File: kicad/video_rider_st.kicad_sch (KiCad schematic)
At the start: 37 parts, among them J1 F3311A7H121020E200, J2 F3311A7H121020E200, J3 Conn_01x02_Male, J4 Conn_01x03_Male, J5 F3311A7H121020E200, J6 F3311A7H121020E200, J7 Conn_01x06_Male, U1 ST_SHIFTER_PHY, U10 ST_GLUE_SOCKET, U2 ST_SHIFTER_SOCKET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

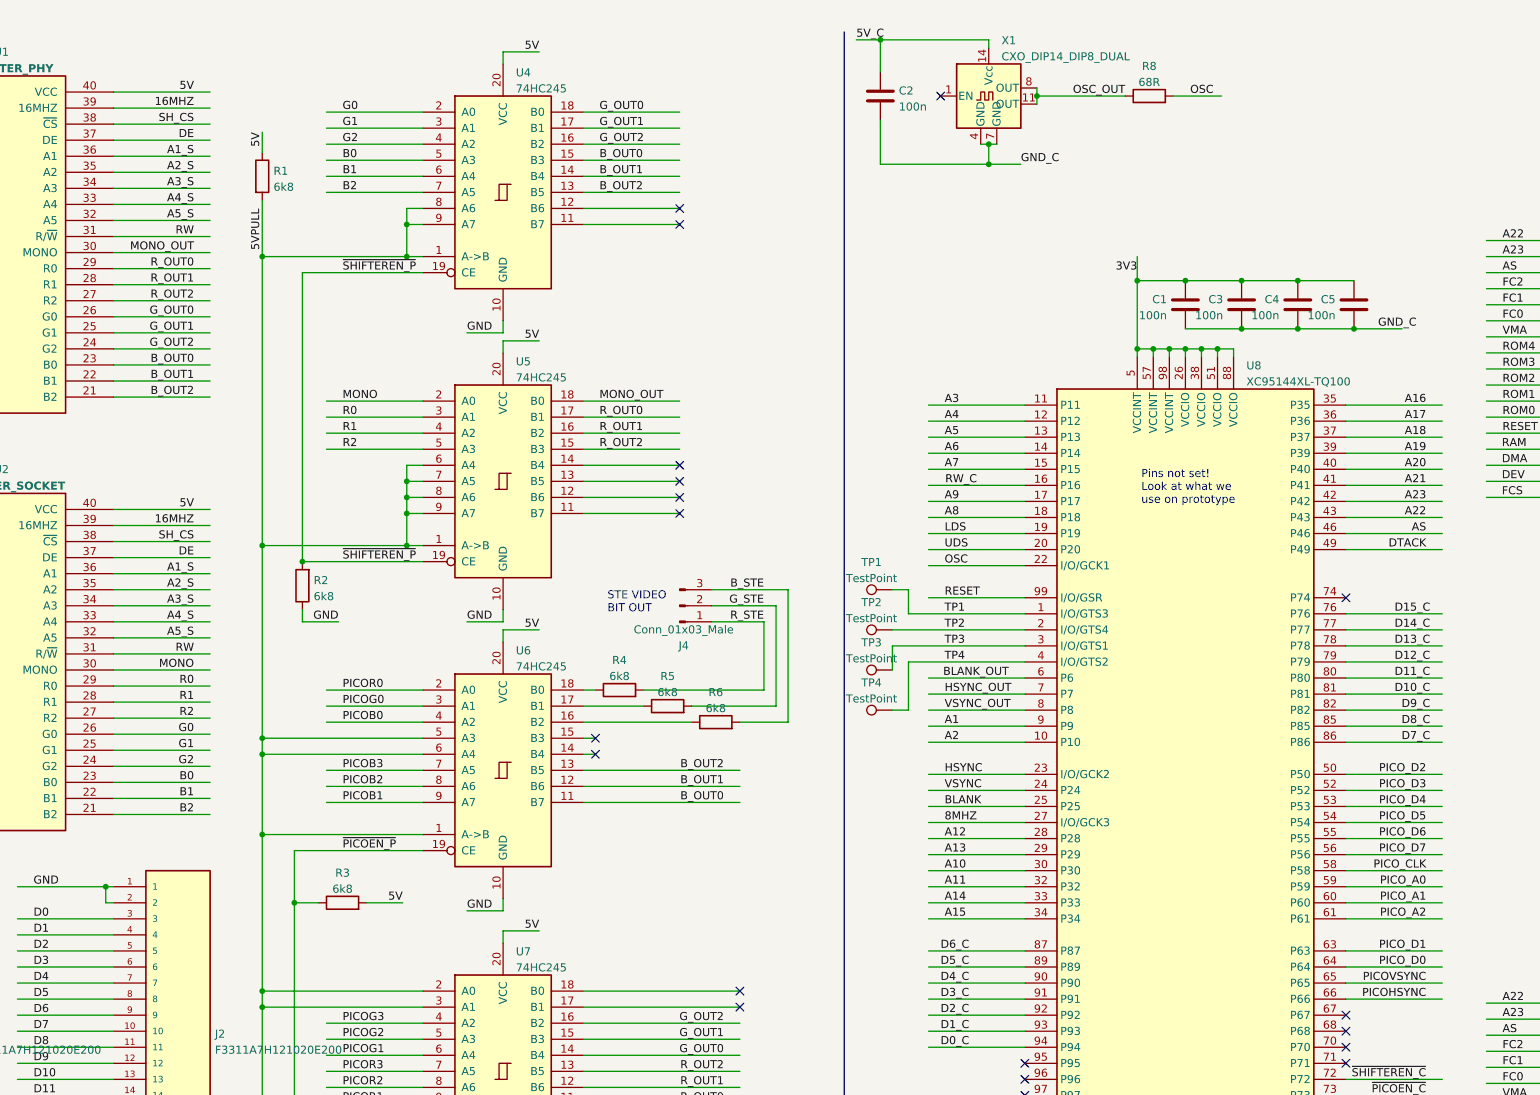
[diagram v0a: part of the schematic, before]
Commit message: Just about ready to order, but need to check the dual dip library.
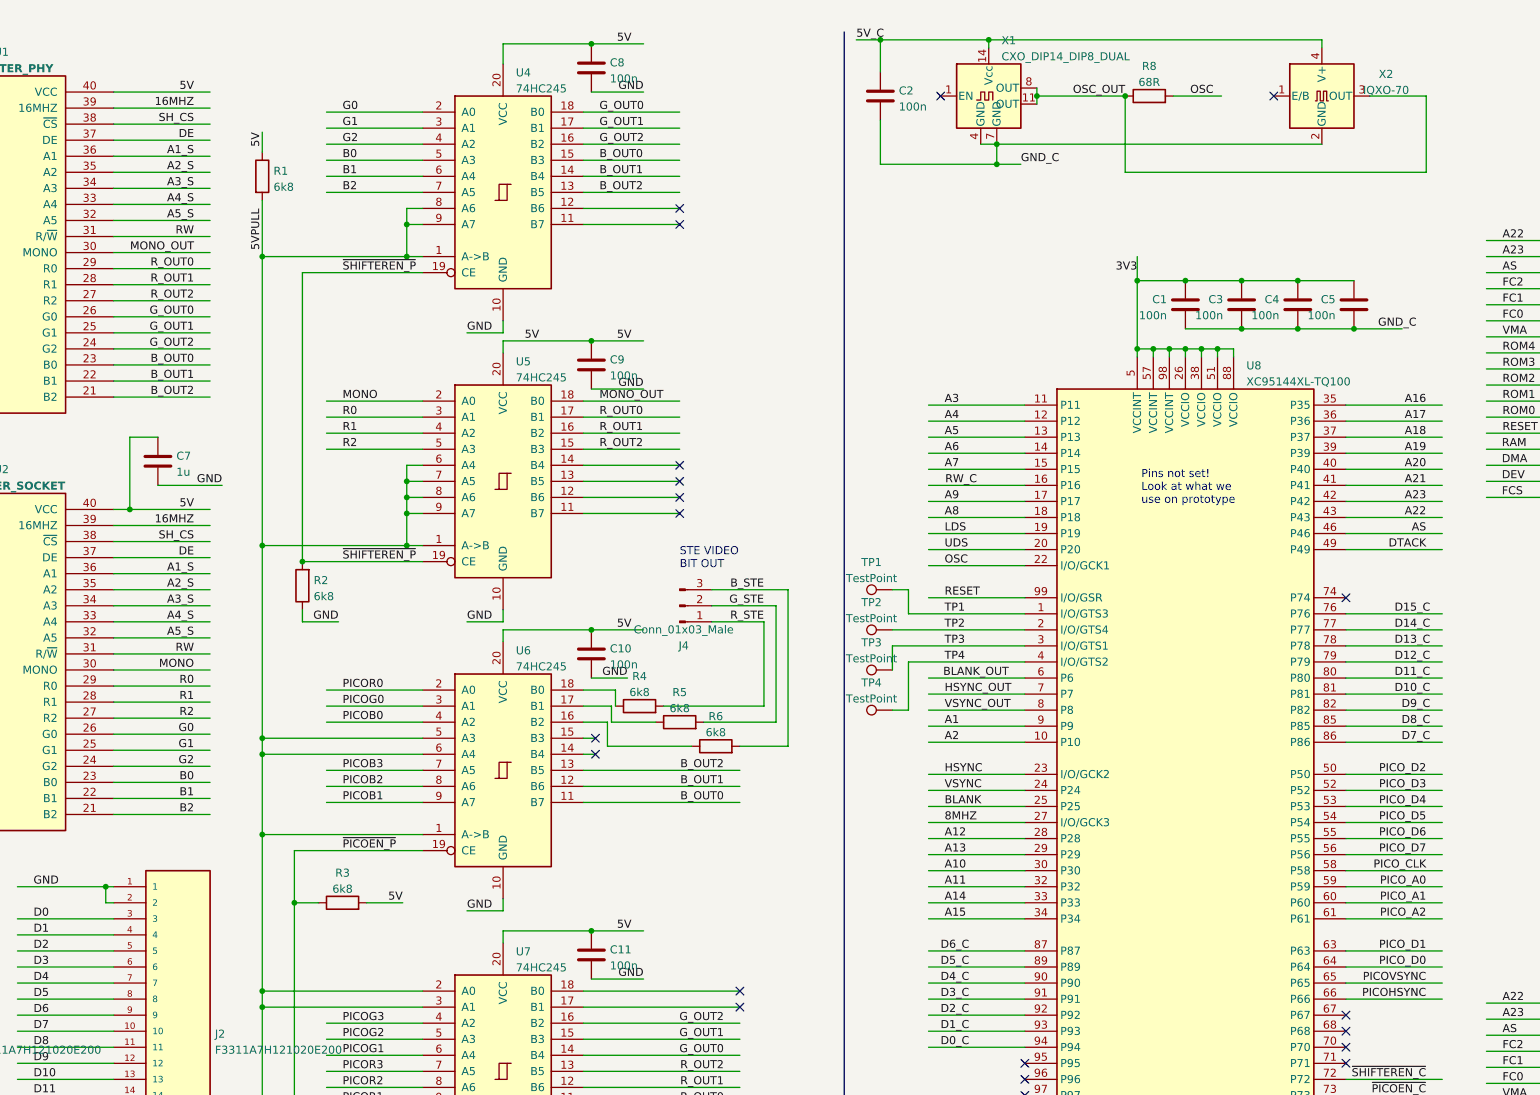
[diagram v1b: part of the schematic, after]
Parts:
- added C10, C11, C8, C9: 100n, Capacitor_SMD:C_0805_2012Metric_Pad1.18x1.45mm_HandSolder, symbol Device:C
- added C7: 1u, Capacitor_SMD:C_0805_2012Metric_Pad1.18x1.45mm_HandSolder, symbol Device:C
- added X2: IQXO-70, Oscillator:Oscillator_SMD_IQD_IQXO70-4Pin_7.5x5.0mm, symbol Oscillator:IQXO-70
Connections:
- net 5V: now also C10.1, C11.1, C7.1, C8.1, C9.1
- net 5V_C: now also X2.4 (V+)
- net GND: now also C10.2, C11.2, C7.2, C8.2, C9.2
- net GND_C: now also X2.2 (GND)
- net OSC_OUT: now also X2.3 (OUT)
- no-connect marks 27 -> 28
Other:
- moved on the sheet: R4, R5, R6

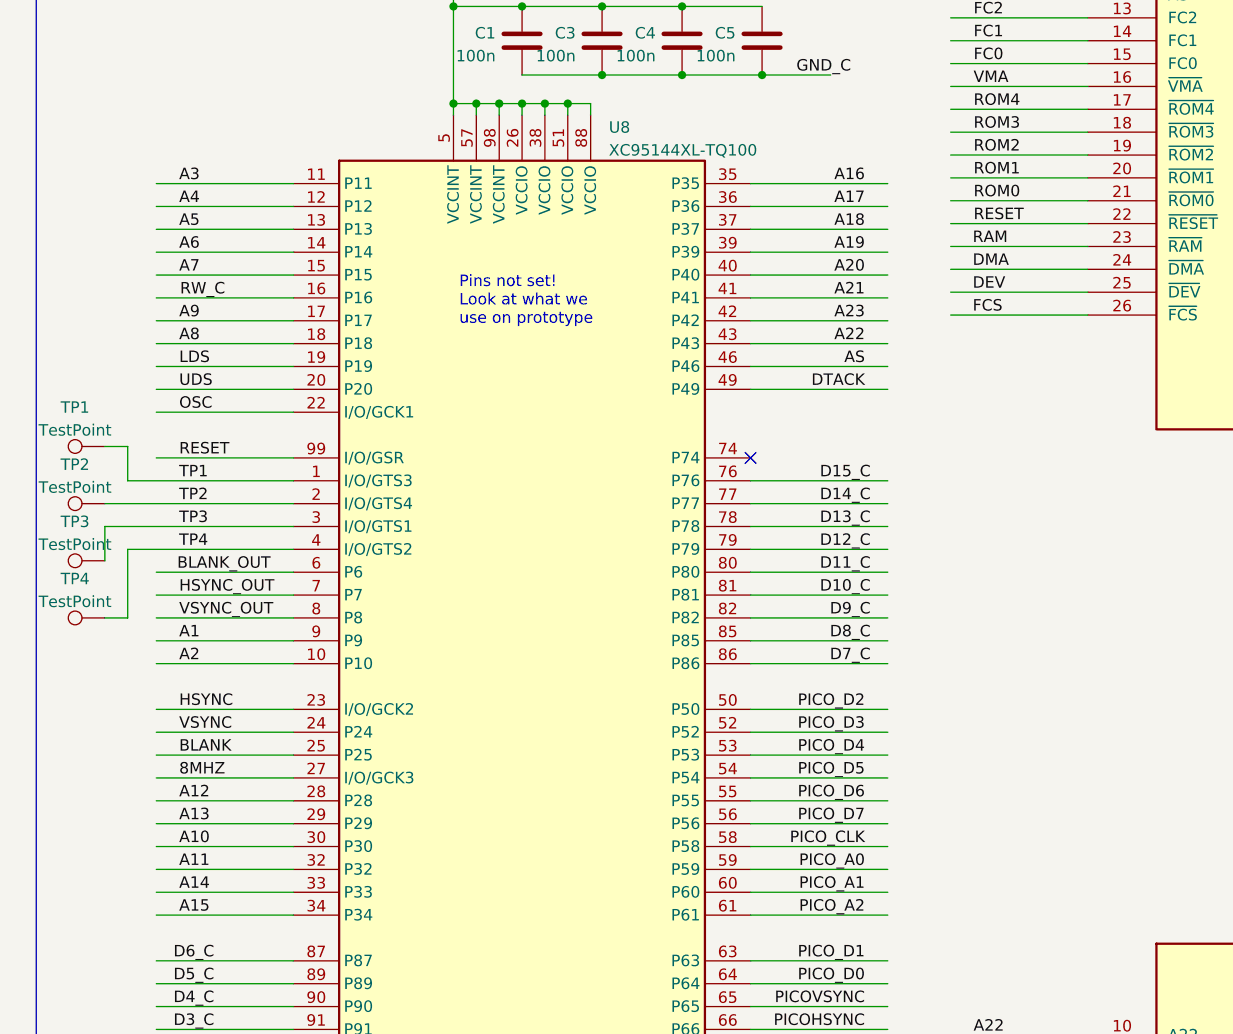
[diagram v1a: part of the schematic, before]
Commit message: Passing DRC with corrected PLCC orientation.
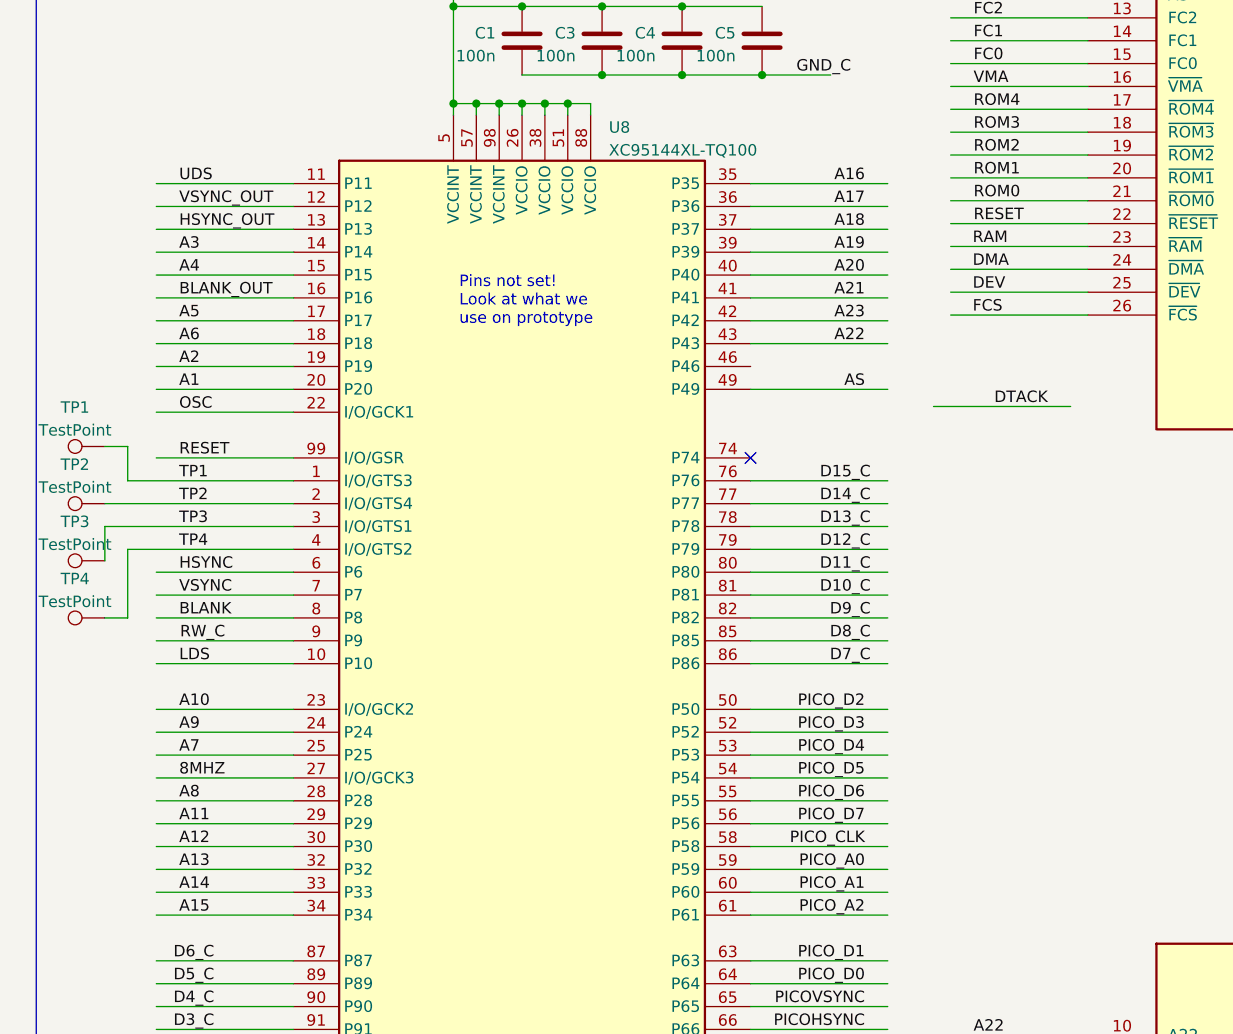
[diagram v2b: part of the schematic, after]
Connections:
- net A1: now also U8.20 (P20); no longer U8.9 (P9)
- net A10: now also U8.23 (I/O/GCK2); no longer U8.30 (P30)
- net A11: now also U8.29 (P29); no longer U8.32 (P32)
- net A12: now also U8.30 (P30); no longer U8.28 (P28)
- net A13: now also U8.32 (P32); no longer U8.29 (P29)
- net A2: now also U8.19 (P19); no longer U8.10 (P10)
- net A3: now also U8.14 (P14); no longer U8.11 (P11)
- net A4: now also U8.15 (P15); no longer U8.12 (P12)
- net A5: now also U8.17 (P17); no longer U8.13 (P13)
- net A6: now also U8.18 (P18); no longer U8.14 (P14)
- net A7: now also U8.25 (P25); no longer U8.15 (P15)
- net A8: now also U8.28 (P28); no longer U8.18 (P18)
- net A9: now also U8.24 (P24); no longer U8.17 (P17)
- net AS: now also U8.49 (P49); no longer U8.46 (P46)
- net BLANK: now also U8.8 (P8); no longer U8.25 (P25)
- net BLANK_OUT: now also U8.16 (P16); no longer U8.6 (P6)
- net DTACK: no longer U8.49 (P49)
- net HSYNC: now also U8.6 (P6); no longer U8.23 (I/O/GCK2)
- net HSYNC_OUT: now also U8.13 (P13); no longer U8.7 (P7)
- net LDS: now also U8.10 (P10); no longer U8.19 (P19)
- net RW_C: now also U8.9 (P9); no longer U8.16 (P16)
- net UDS: now also U8.11 (P11); no longer U8.20 (P20)
- net VSYNC: now also U8.7 (P7); no longer U8.24 (P24)
- net VSYNC_OUT: now also U8.12 (P12); no longer U8.8 (P8)
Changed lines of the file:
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@@
     (stroke (width 0) (type default) (color 0 0 0 0))
   )
-  (wire (pts (xy 269.875 95.25) (xy 285.115 95.25))
+  (wire (pts (xy 269.875 97.79) (xy 285.115 97.79))
     (stroke (width 0) (type default) (color 0 0 0 0))
   )
@@
     (stroke (width 0) (type default) (color 0 0 0 0))
   )
-  (wire (pts (xy 269.875 97.79) (xy 285.115 97.79))
+  (wire (pts (xy 290.195 99.695) (xy 305.435 99.695))
     (stroke (width 0) (type default) (color 0 0 0 0))
   )
@@
     (effects (font (size 1.27 1.27)) (justify right bottom))
   )
-  (label "A12" (at 206.375 143.51 0)
+  (label "A12" (at 206.375 148.59 0)
     (effects (font (size 1.27 1.27)) (justify left bottom))
   )
@@
     (effects (font (size 1.27 1.27)) (justify left bottom))
   )
-  (label "A2" (at 206.375 128.27 0)
+  (label "A2" (at 206.375 95.25 0)
     (effects (font (size 1.27 1.27)) (justify left bottom))
   )
@@
     (effects (font (size 1.27 1.27)) (justify left bottom))
   )
-  (label "BLANK_OUT" (at 216.535 118.11 180)
-    (effects (font (size 1.27 1.27)) (justify right bottom))
+  (label "BLANK_OUT" (at 206.375 87.63 0)
+    (effects (font (size 1.27 1.27)) (justify left bottom))
   )
   (label "D5" (at 62.23 168.91 0)
@@
     (effects (font (size 1.27 1.27)) (justify left bottom))
   )
-  (label "A11" (at 206.375 151.13 0)
+  (label "A11" (at 206.375 146.05 0)
     (effects (font (size 1.27 1.27)) (justify left bottom))
   )
@@
     (effects (font (size 1.27 1.27)) (justify left bottom))
   )
-  (label "HSYNC" (at 206.375 133.35 0)
+  (label "HSYNC" (at 206.375 118.11 0)
     (effects (font (size 1.27 1.27)) (justify left bottom))
   )
@@
     (effects (font (size 1.27 1.27)) (justify left bottom))
   )
-  (label "AS" (at 282.575 95.25 180)
+  (label "AS" (at 282.575 97.79 180)
     (effects (font (size 1.27 1.27)) (justify right bottom))
   )
@@
     (effects (font (size 1.27 1.27)) (justify right bottom))
   )
-  (label "BLANK" (at 206.375 138.43 0)
+  (label "BLANK" (at 206.375 123.19 0)
     (effects (font (size 1.27 1.27)) (justify left bottom))
   )
@@
     (effects (font (size 1.27 1.27)) (justify left bottom))
   )
-  (label "A1" (at 206.375 125.73 0)
+  (label "A1" (at 206.375 97.79 0)
     (effects (font (size 1.27 1.27)) (justify left bottom))
   )
@@
     (effects (font (size 1.27 1.27)) (justify left bottom))
   )
-  (label "A4" (at 206.375 77.47 0)
+  (label "A4" (at 206.375 85.09 0)
     (effects (font (size 1.27 1.27)) (justify left bottom))
   )
@@
     (effects (font (size 1.27 1.27)) (justify right bottom))
   )
-  (label "VSYNC" (at 206.375 135.89 0)
+  (label "VSYNC" (at 206.375 120.65 0)
     (effects (font (size 1.27 1.27)) (justify left bottom))
   )
@@
     (effects (font (size 1.27 1.27)) (justify left bottom))
   )
-  (label "A5" (at 206.375 80.01 0)
+  (label "A5" (at 206.375 90.17 0)
     (effects (font (size 1.27 1.27)) (justify left bottom))
   )
@@
     (effects (font (size 1.27 1.27)) (justify left bottom))
   )
-  (label "VSYNC_OUT" (at 206.375 123.19 0)
+  (label "VSYNC_OUT" (at 206.375 77.47 0)
     (effects (font (size 1.27 1.27)) (justify left bottom))
   )
@@
     (effects (font (size 1.27 1.27)) (justify right bottom))
   )
-  (label "RW_C" (at 206.4754 87.63 0)
+  (label "RW_C" (at 206.4754 125.73 0)
     (effects (font (size 1.27 1.27)) (justify left bottom))
   )
-  (label "UDS" (at 206.375 97.79 0)
+  (label "UDS" (at 206.375 74.93 0)
     (effects (font (size 1.27 1.27)) (justify left bottom))
   )
@@
     (effects (font (size 1.27 1.27)) (justify left bottom))
   )
-  (label "A9" (at 206.375 90.17 0)
+  (label "A9" (at 206.375 135.89 0)
     (effects (font (size 1.27 1.27)) (justify left bottom))
   )
@@
     (effects (font (size 1.27 1.27)) (justify right bottom))
   )
-  (label "A10" (at 206.375 148.59 0)
+  (label "A10" (at 206.375 133.35 0)
     (effects (font (size 1.27 1.27)) (justify left bottom))
   )
@@
     (effects (font (size 1.27 1.27)) (justify right bottom))
   )
-  (label "LDS" (at 206.375 95.25 0)
+  (label "LDS" (at 206.375 128.27 0)
     (effects (font (size 1.27 1.27)) (justify left bottom))
   )
@@
     (effects (font (size 1.27 1.27)) (justify right bottom))
   )
-  (label "HSYNC_OUT" (at 206.375 120.65 0)
+  (label "HSYNC_OUT" (at 206.375 80.01 0)
     (effects (font (size 1.27 1.27)) (justify left bottom))
   )
@@
     (effects (font (size 1.27 1.27)) (justify right bottom))
   )
-  (label "A6" (at 206.375 82.55 0)
+  (label "A6" (at 206.375 92.71 0)
     (effects (font (size 1.27 1.27)) (justify left bottom))
   )
@@
     (effects (font (size 1.27 1.27)) (justify right bottom))
   )
-  (label "A3" (at 206.375 74.93 0)
+  (label "A3" (at 206.375 82.55 0)
     (effects (font (size 1.27 1.27)) (justify left bottom))
   )
@@
     (effects (font (size 1.27 1.27)) (justify left bottom))
   )
-  (label "A13" (at 206.375 146.05 0)
+  (label "A13" (at 206.375 151.13 0)
     (effects (font (size 1.27 1.27)) (justify left bottom))
   )
@@
     (effects (font (size 1.27 1.27)) (justify left bottom))
   )
-  (label "A7" (at 206.375 85.09 0)
+  (label "A7" (at 206.375 138.43 0)
     (effects (font (size 1.27 1.27)) (justify left bottom))
   )
@@
     (effects (font (size 1.27 1.27)) (justify right bottom))
   )
-  (label "A8" (at 206.375 92.71 0)
+  (label "A8" (at 206.375 143.51 0)
     (effects (font (size 1.27 1.27)) (justify left bottom))
   )
@@
     (effects (font (size 1.27 1.27)) (justify right bottom))
   )
-  (label "DTACK" (at 282.575 97.79 180)
+  (label "DTACK" (at 302.895 99.695 180)
     (effects (font (size 1.27 1.27)) (justify right bottom))
   )
